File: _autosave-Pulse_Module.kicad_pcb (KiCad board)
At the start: 2 copper layers, 100.2 x 70.9 mm, 61 parts, among them CON1 AVR-ISP-10, CON2 AVR-JTAG-10, CON3 BARREL_JACK, IC1 ATMEGA1280-A, P1 CONN_02X20, P2 USB_OTG, P3 CONN_01X03, P4 CONN_01X03, SW1 SW_PUSH, U1 74HCT541_PWR, U2 PL2303, U6 WS2812, U7 WS2812, U8 WS2812, X1 CRYSTAL, Y1 CRYSTAL

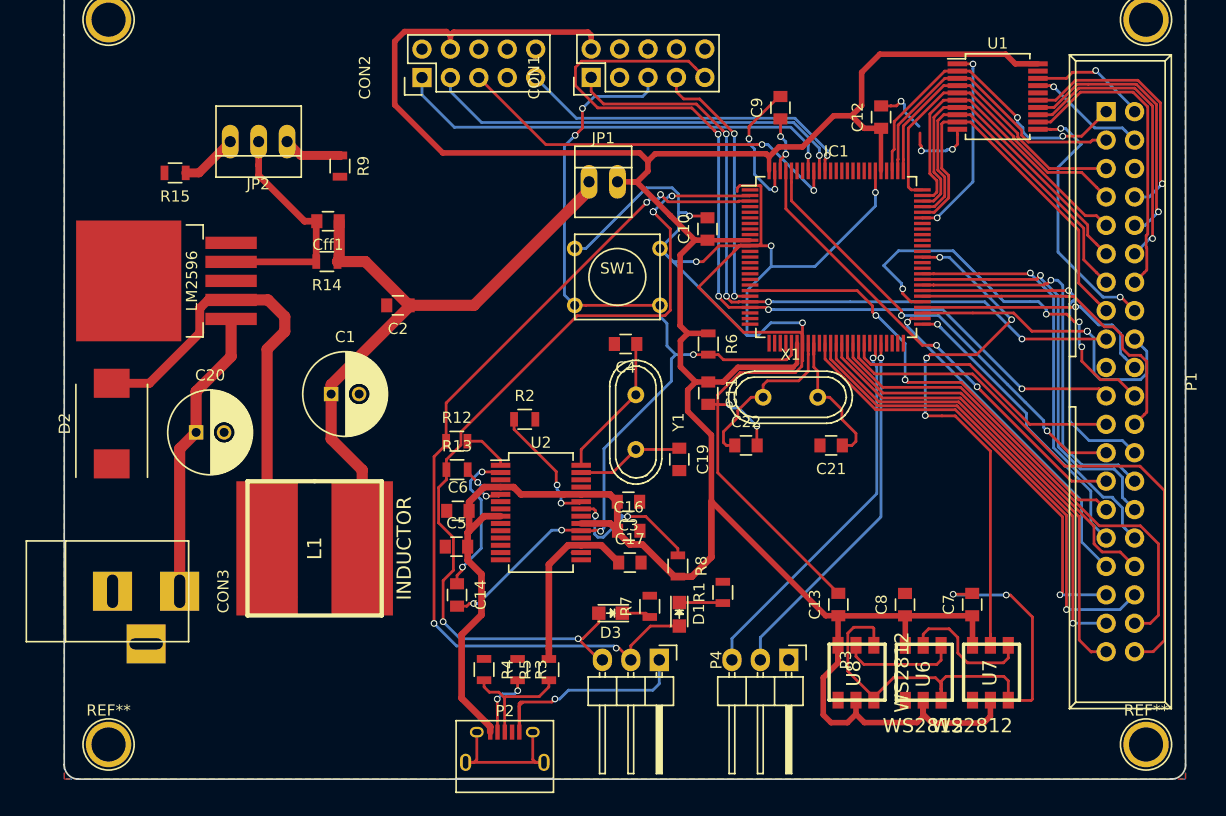
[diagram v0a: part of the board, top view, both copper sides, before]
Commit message: исправление согласно замечаниям, переразведена PL2303
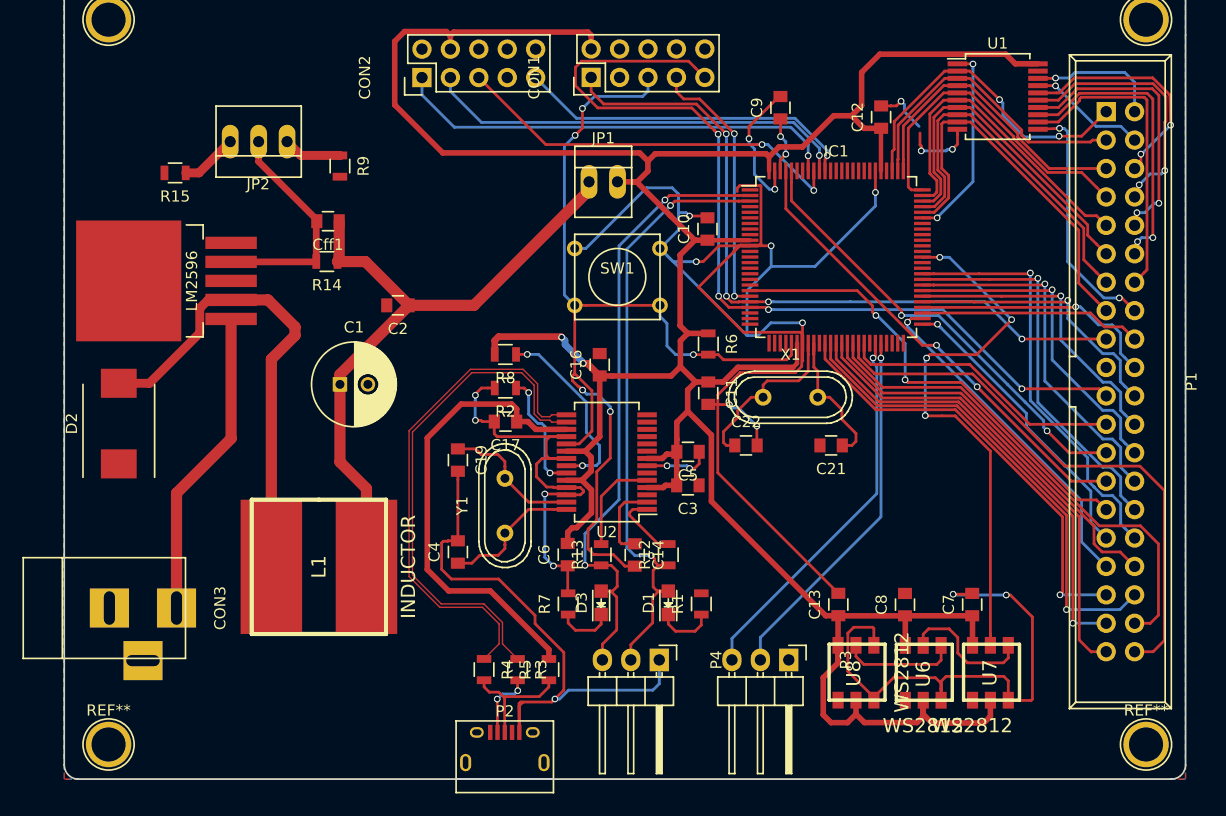
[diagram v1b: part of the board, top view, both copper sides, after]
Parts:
- removed C20: 470uF, Capacitors_ThroughHole:C_Radial_D7.5_L11.2_P2.5
- moved R8 24.4 mm to (142.1, 111.8), turned to 180 degrees
- moved C4 23.9 mm to (137.9, 129.5), turned to 90 degrees
- moved C5 22.4 mm to (158.5, 120.5), turned to 180 degrees
- moved R12 21.5 mm to (156.7, 129.7), turned to 90 degrees
- moved C19 19.8 mm to (137.9, 121.3)
- moved C17 16.8 mm to (142.2, 117.8), turned to 180 degrees
- moved C14 16.3 mm to (153.7, 129.8)
- moved C16 15.1 mm to (150.6, 112.8), turned to 90 degrees
- moved R13 15.0 mm to (150.7, 129.7), turned to 90 degrees
- moved Y1 13.9 mm to (142.1, 125.3), turned to 90 degrees
- moved C6 10.6 mm to (147.7, 129.7), turned to 90 degrees
- moved U2 7.41 mm to (151.2, 121.5), turned to 180 degrees
- moved R7 7.29 mm to (147.8, 134.1)
- moved C3 5.51 mm to (158.4, 123.5)
- moved R2 3.29 mm to (142.1, 114.8), turned to 180 degrees
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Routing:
- net GND: track 235.8 -> 312.6 mm, vias 15 -> 21
- net /Sheet56DEE0DD/Sheet570520A0/D+: track 0.65 -> 46.8 mm
- net /Sheet56DEE0DD/Sheet570520A0/D-: track 0.83 -> 45.7 mm
- net +3V3: track 16.0 -> 41.7 mm
- net /Sheet56DEE0DD/Sheet570520A0/TXD: track 80.7 -> 55.6 mm, vias 4 -> 2
- net /Sheet56DEE0DD/Sheet570520A0/RXD: track 79.6 -> 57.2 mm, vias 5 -> 2
- net /Sheet56DEE0DD/A2: track 0.77 -> 21.0 mm, vias 0 -> 2
- net Net-(P2-Pad6): track 14.4 -> 0.30 mm
- net /Sheet56DEE0DD/A10: track 35.8 -> 24.6 mm, vias 4 -> 1
- net +5V: track 285.6 -> 275.8 mm, vias 0 -> 2
- net /Sheet56DEE0DD/A8: track 28.1 -> 19.9 mm, vias 2 -> 0
- net Net-(C14-Pad1): track 13.5 -> 7.17 mm, vias 2 -> 0
- net Net-(R13-Pad2): track 4.60 -> 8.95 mm, vias 2 -> 0
- net /Sheet56DEE0DD/Sheet570520A0/RESET: track 85.0 -> 88.8 mm, vias 6 -> 5
- net Net-(R8-Pad1): track 13.9 -> 17.0 mm
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
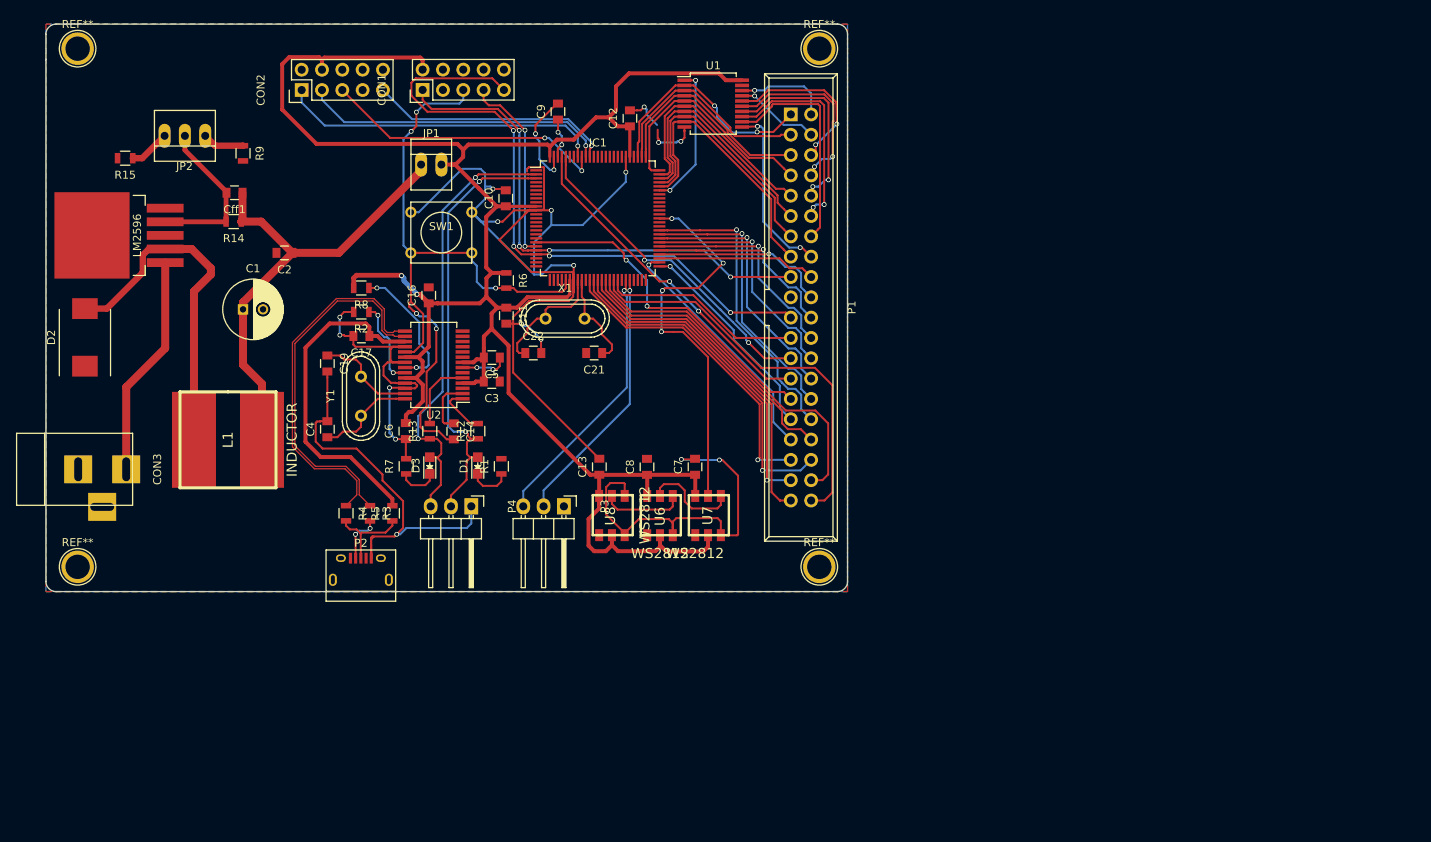
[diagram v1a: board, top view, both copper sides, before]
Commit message: подключение питания LMки от USB
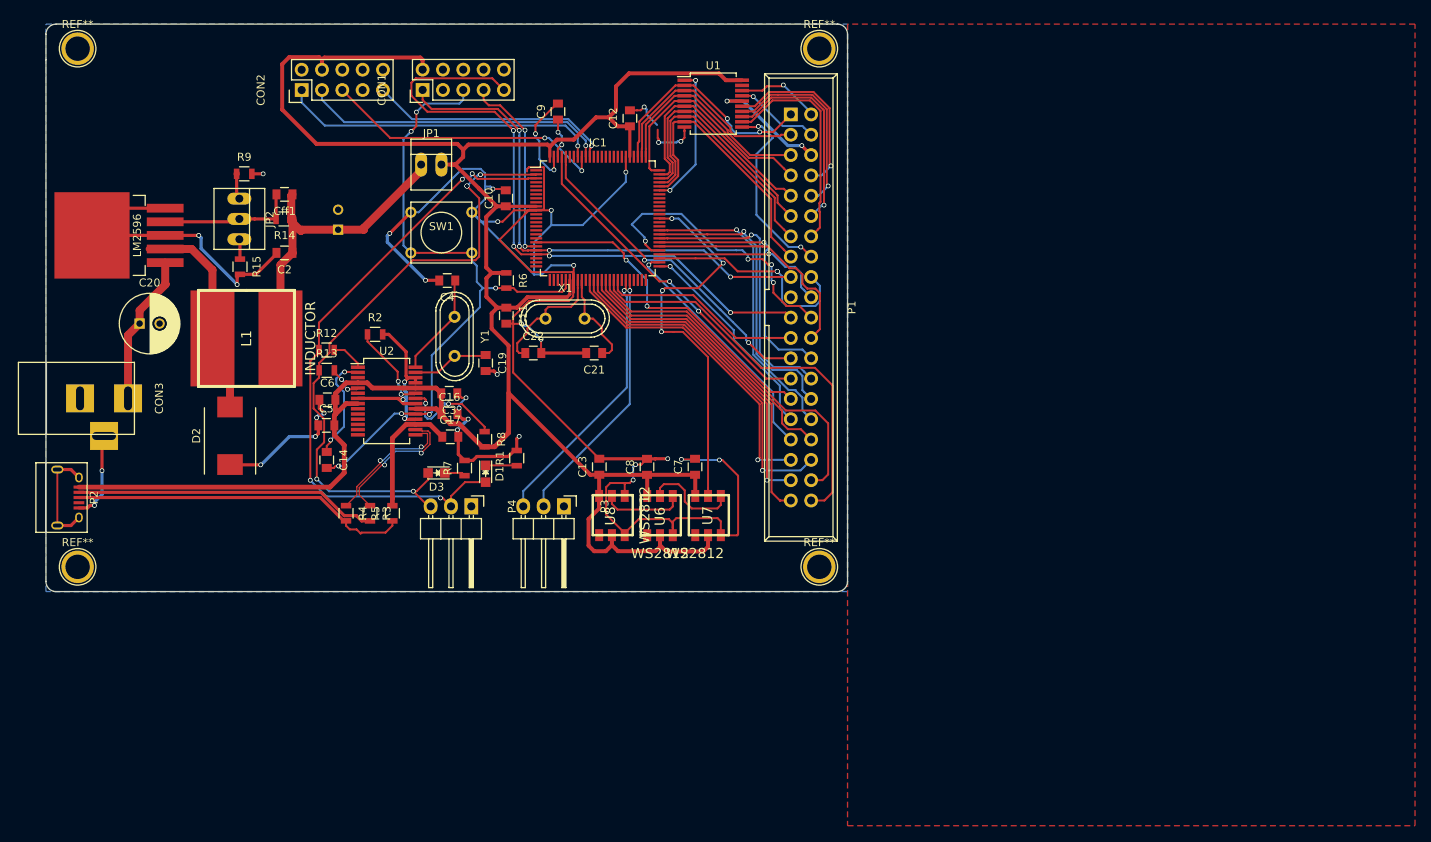
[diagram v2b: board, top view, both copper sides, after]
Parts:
- added C20: 470uF, Capacitors_ThroughHole:C_Radial_D7.5_L11.2_P2.5, F.Cu at (114.4, 116.3)
- C1: moved to B.Cu
- moved P2 37.9 mm to (105.3, 138.0), turned to 270 degrees
- moved R8 24.4 mm to (157.6, 130.7), turned to 270 degrees
- moved C4 23.9 mm to (152.9, 110.9), turned to 180 degrees
- moved C5 22.4 mm to (137.8, 129.0), turned to 0 degrees
- moved D2 21.9 mm to (125.7, 130.3)
- moved R12 21.5 mm to (137.8, 119.6), turned to 0 degrees
- moved C19 19.8 mm to (157.7, 121.2)
- moved R15 19.7 mm to (127.0, 109.2), turned to 270 degrees
- moved C17 16.8 mm to (153.3, 130.4), turned to 0 degrees
- moved C14 16.3 mm to (137.8, 133.3)
- moved C1 15.5 mm to (139.2, 104.5), turned to 90 degrees
- moved C16 15.1 mm to (153.2, 127.6), turned to 0 degrees
- moved R13 15.0 mm to (137.8, 122.1), turned to 0 degrees
- moved Y1 13.9 mm to (153.8, 117.9), turned to 270 degrees
- moved L1 12.9 mm to (127.8, 118.1)
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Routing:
- net GND: track 312.6 -> 365.0 mm, vias 21 -> 37
- net Net-(P2-Pad2): track 6.06 -> 37.9 mm, vias 2 -> 0
- net Net-(P2-Pad3): track 10.9 -> 42.4 mm
- net +5V: track 275.8 -> 307.1 mm, vias 2 -> 0
- net /Sheet56DEE0DD/Sheet570520A0/D+: track 46.8 -> 17.0 mm, vias 0 -> 2
- net /Sheet56DEE0DD/Sheet570520A0/D-: track 45.7 -> 18.5 mm, vias 0 -> 2
- net +3V3: track 41.7 -> 16.0 mm
- net /Sheet56DEE0DD/Sheet570520A0/TXD: track 55.6 -> 80.7 mm, vias 2 -> 4
- net /Sheet56DEE0DD/Sheet570520A0/RXD: track 57.2 -> 79.6 mm, vias 2 -> 5
- net /Sheet56DEE0DD/Vcc: track 61.0 -> 41.5 mm
- net Net-(D2-Pad2): track 46.2 -> 29.8 mm
- net Net-(P2-Pad6): track 0.30 -> 13.5 mm
- net /Sheet56DEE0DD/A10: track 24.6 -> 35.8 mm, vias 1 -> 4
- net /Sheet56D88A8D/Vin: track 28.1 -> 19.0 mm
- net /Sheet56DEE0DD/A8: track 19.9 -> 28.1 mm, vias 0 -> 2
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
